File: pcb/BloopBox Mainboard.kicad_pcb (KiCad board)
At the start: 4 copper layers, 65 x 44 mm, 57 parts, among them J1 SPKR, J2 Raspberry_Pi, J3 I2C, J4 TailBoard, J5 GPIO, J6 NFCModuleV3, J7 ExtLED, Q1 2N7002, Q2 2N7002, Q3 2N7002, Q4 2N7002, Q5 2N7002, Q6 2N7002, U1 MAX98357

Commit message: feat: prepare files for automatic version numbering
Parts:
- G***, REF**: moved to B.Cu
- moved REF** 23.1 mm to (160.0, 61.2), turned to 180 degrees
- moved G*** 10.4 mm to (140.0, 61.0), turned to 180 degrees
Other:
- board text added: "BloopBox Mainboard ${VERSION} ${DATE}"
- board text added: "BloopBox Mainboard ${VERSION} %{DATE}"
- board text removed: "BloopBox v1.0"

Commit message: feat: more variables
Using more variables to automate stuff
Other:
- board text added: "${TITLE} ${VERSION} ${DATE}"
- board text removed: "BloopBox Mainboard ${VERSION} ${DATE}"
- board text removed: "BloopBox Mainboard ${VERSION} %{DATE}"
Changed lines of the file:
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@@
     )
   )
+  (property "DATE" "~DATE~")
+  (property "VERSION" "~VERSION~")
   (net 0 "")
   (net 1 "/OUTP")
@@
     (effects (font (size 1 1) (thickness 0.15)) (justify right mirror))
   )
-  (gr_text "BloopBox Mainboard\n${VERSION} %{DATE}" (at 150 55) (layer "B.SilkS")
+  (gr_text "${TITLE}\n${VERSION} ${DATE}" (at 150 55) (layer "B.SilkS")
     (effects (font (size 1.2 1.2) (thickness 0.2)) (justify mirror))
   )
@@
     (effects (font (size 0.8 0.8) (thickness 0.15)))
   )
-  (gr_text "BloopBox Mainboard\n${VERSION} ${DATE}" (at 150 42) (layer "F.SilkS")
+  (gr_text "${TITLE}\n${VERSION} ${DATE}" (at 150 42) (layer "F.SilkS")
     (effects (font (size 1.2 1.2) (thickness 0.2)))
   )

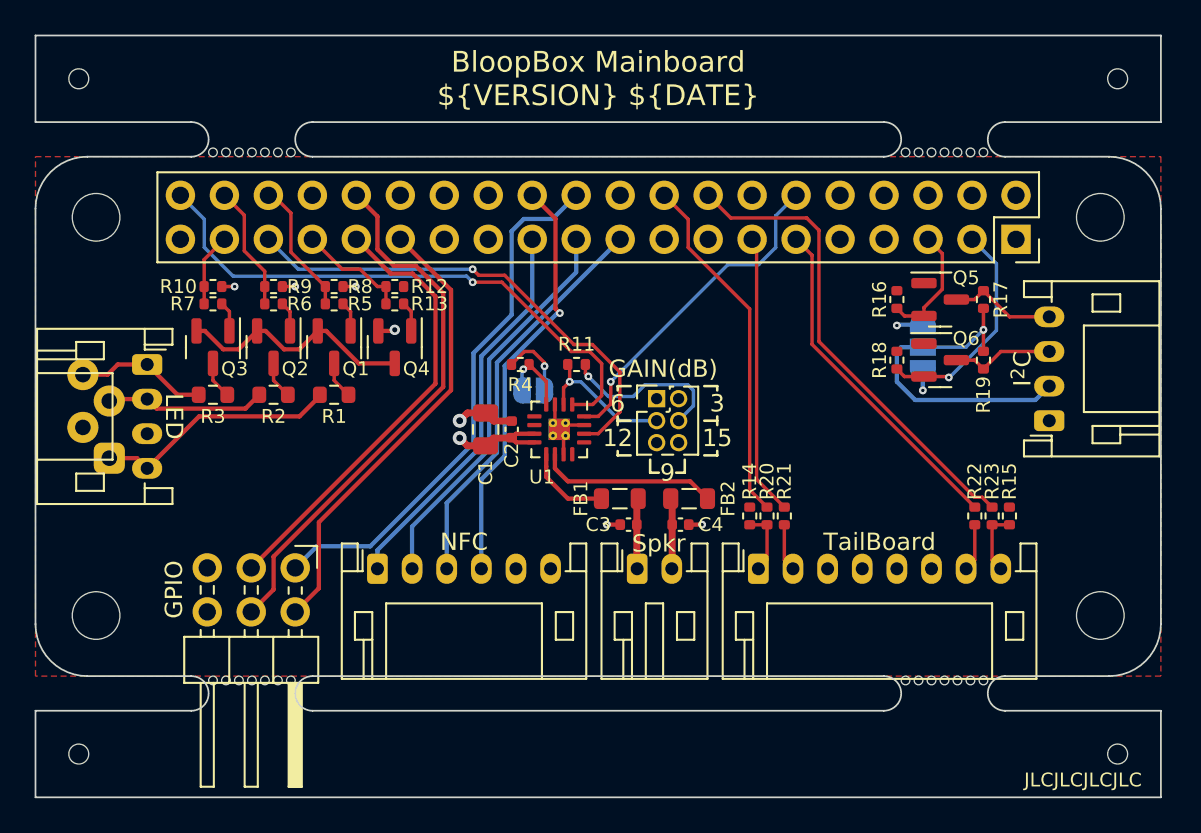
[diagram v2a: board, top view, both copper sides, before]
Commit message: feat: add UART to GPIO-Header
Adding the UART TX and RX pins to the GPIO header for debugging console access
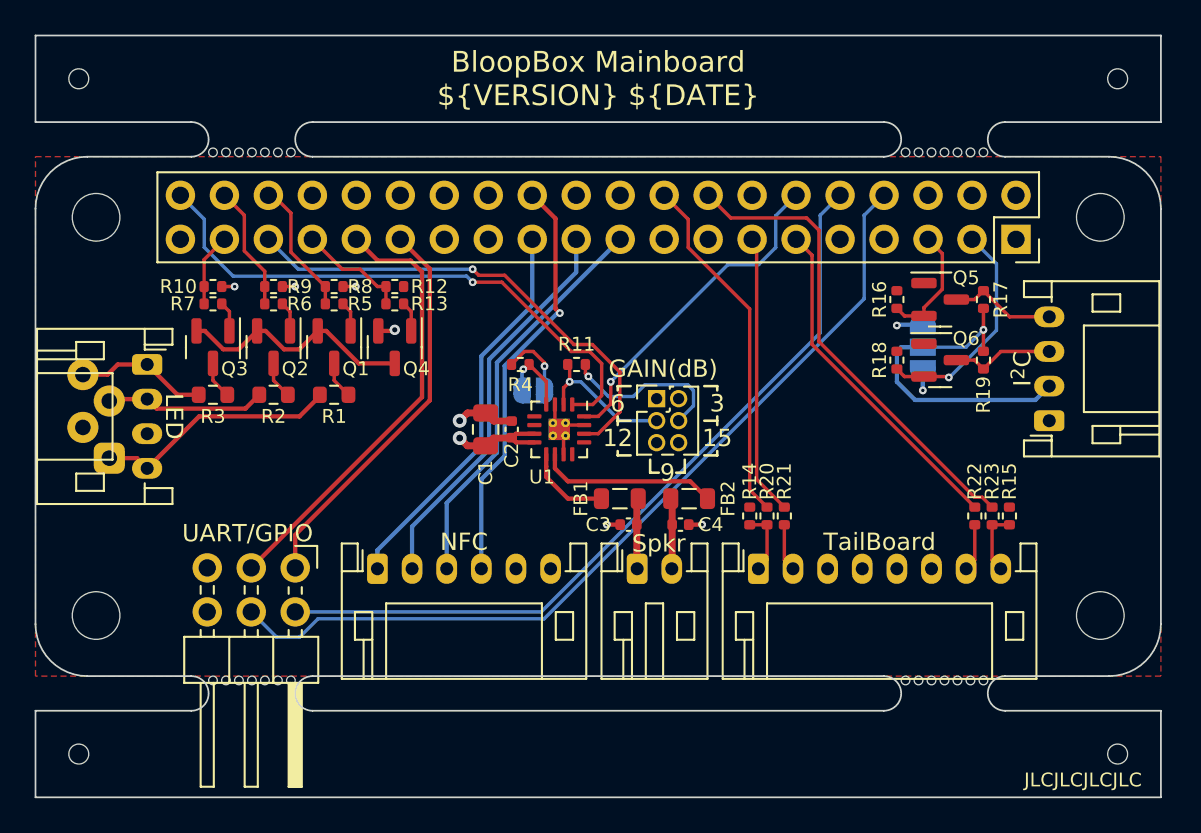
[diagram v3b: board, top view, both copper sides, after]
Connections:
- net /GPIO3 renamed /GPIO6
- J2 pad 10: unconnected-(J2-Pad10) -> /RX
- J2 pad 22: /GPIO1 -> unconnected-(J2-Pad22)
- J2 pad 29: /GPIO2 -> /GPIO5
- J2 pad 32: /GPIO4 -> unconnected-(J2-Pad32)
- J2 pad 8: unconnected-(J2-Pad8) -> /TX
- J5 pad 1: /GPIO1 -> /GPIO5
- J5 pad 2: /GPIO2 -> /RX
- J5 pad 4: /GPIO4 -> /TX
- J5 pad 5: GND -> +3V3
- J5 pad 6: +3V3 -> GND
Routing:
- net /TX: track 0.00 -> 50.6 mm
- net /RX: track 0.00 -> 45.4 mm
- net /GPIO4: track 31.5 -> 0.00 mm
- net /GPIO1: track 31.0 -> 0.00 mm
- net /GPIO2: track 26.5 -> 0.00 mm
- net /GPIO5: track 0.00 -> 22.9 mm
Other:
- board text added: "05"
- board text added: "06"
- board text added: "RX"
- board text added: "TX"
- board text added: "UART/GPIO"
- board text removed: "06 12"
- board text removed: "25 05"
- board text removed: "GPIO"
- board text removed: "IO3"
- board text removed: "IO4"

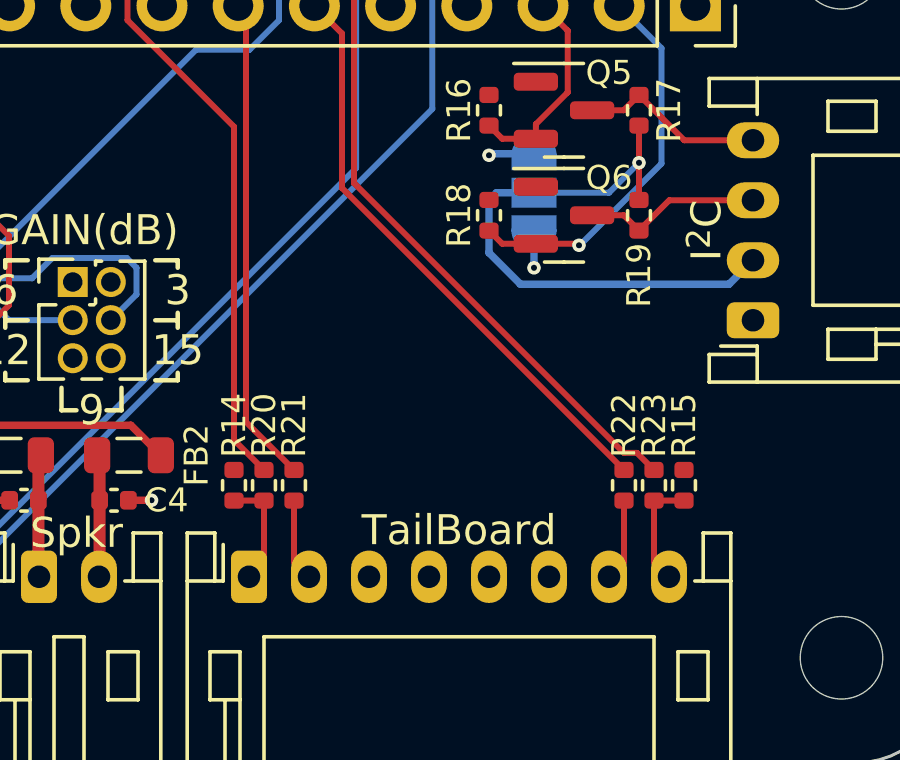
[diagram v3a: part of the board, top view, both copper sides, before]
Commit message: fix: remove Tailboard IO protection resistors
After removing the PD controller from the tailboard, the LEDs are directly connected to the mainboard so the protection resistors had to go
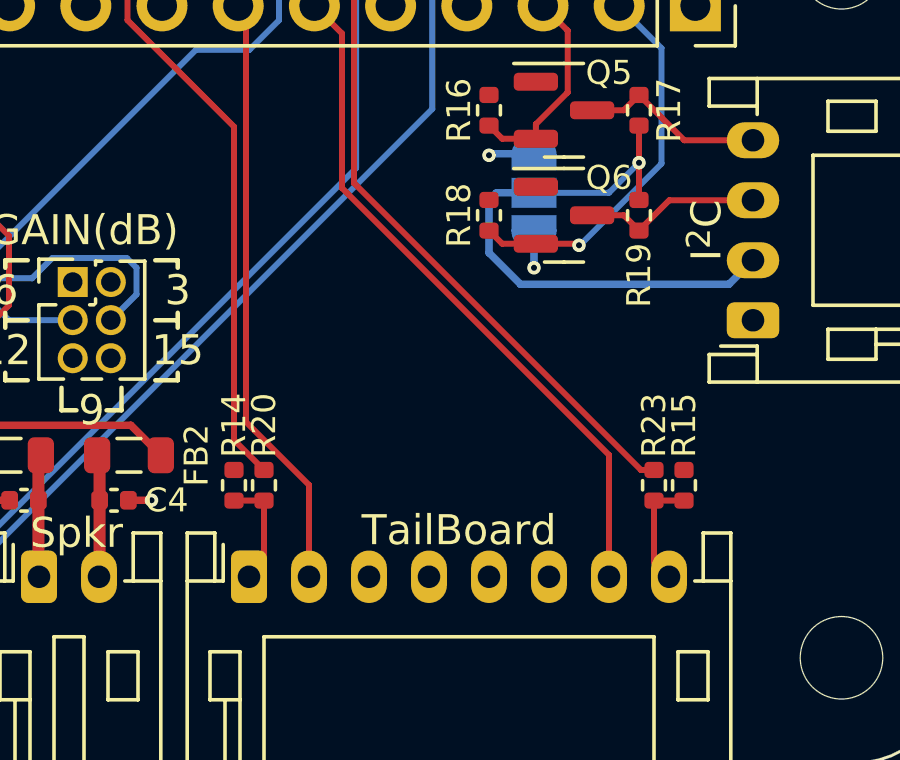
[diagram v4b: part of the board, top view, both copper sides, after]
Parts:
- removed R21, R22: 1k, Resistor_SMD:R_0402_1005Metric
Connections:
- J4 pad 2: /Tail2 -> /Tail_IO1
- J4 pad 7: /Tail7 -> /Tail_IO2
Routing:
- net /Tail_IO1: track 16.2 -> 20.0 mm
- net /Tail_IO2: track 19.7 -> 23.1 mm
- net /Tail7: track 2.75 -> 0.00 mm
- net /Tail2: track 2.75 -> 0.00 mm

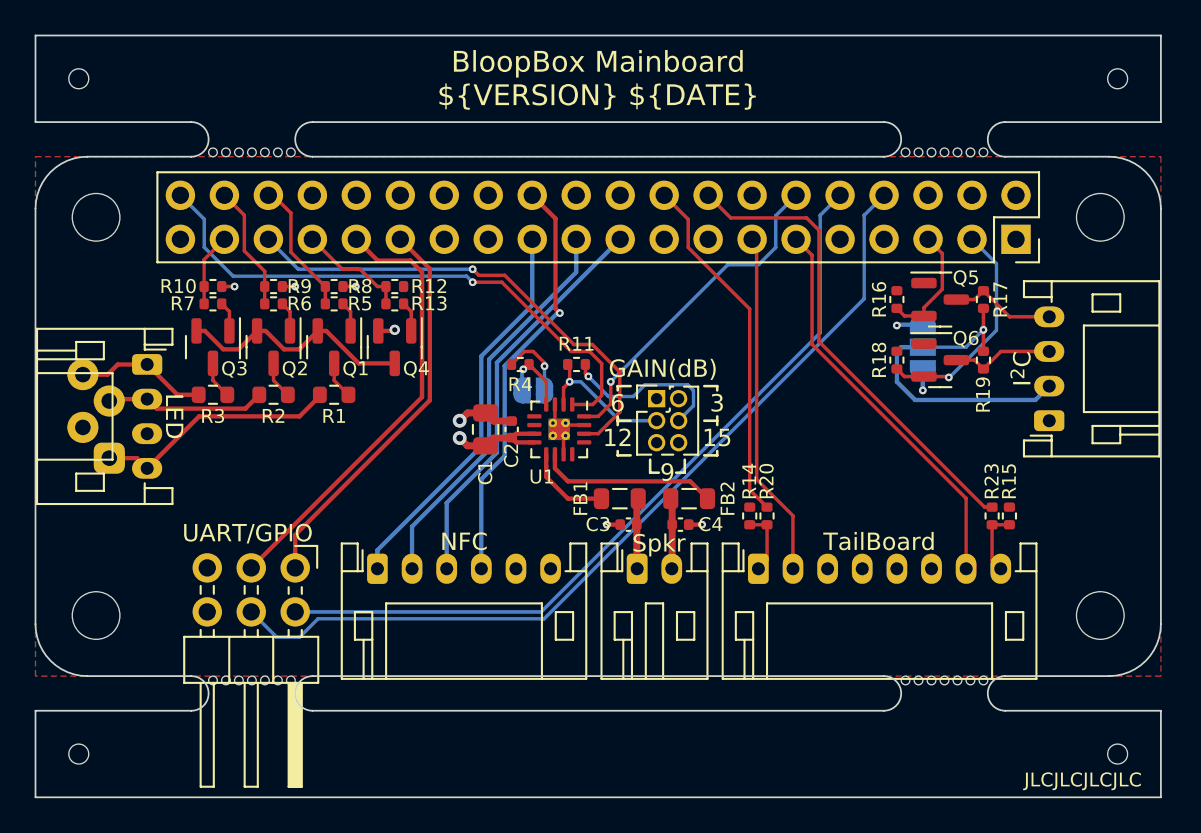
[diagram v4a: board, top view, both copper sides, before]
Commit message: feat!: change NFC connector to RC522 pinout
Switch the NFC-connector from the PN532 module to the RC522 since the PN532 works not reliable with NTAG
Connect IRQ and RST lines while doing so
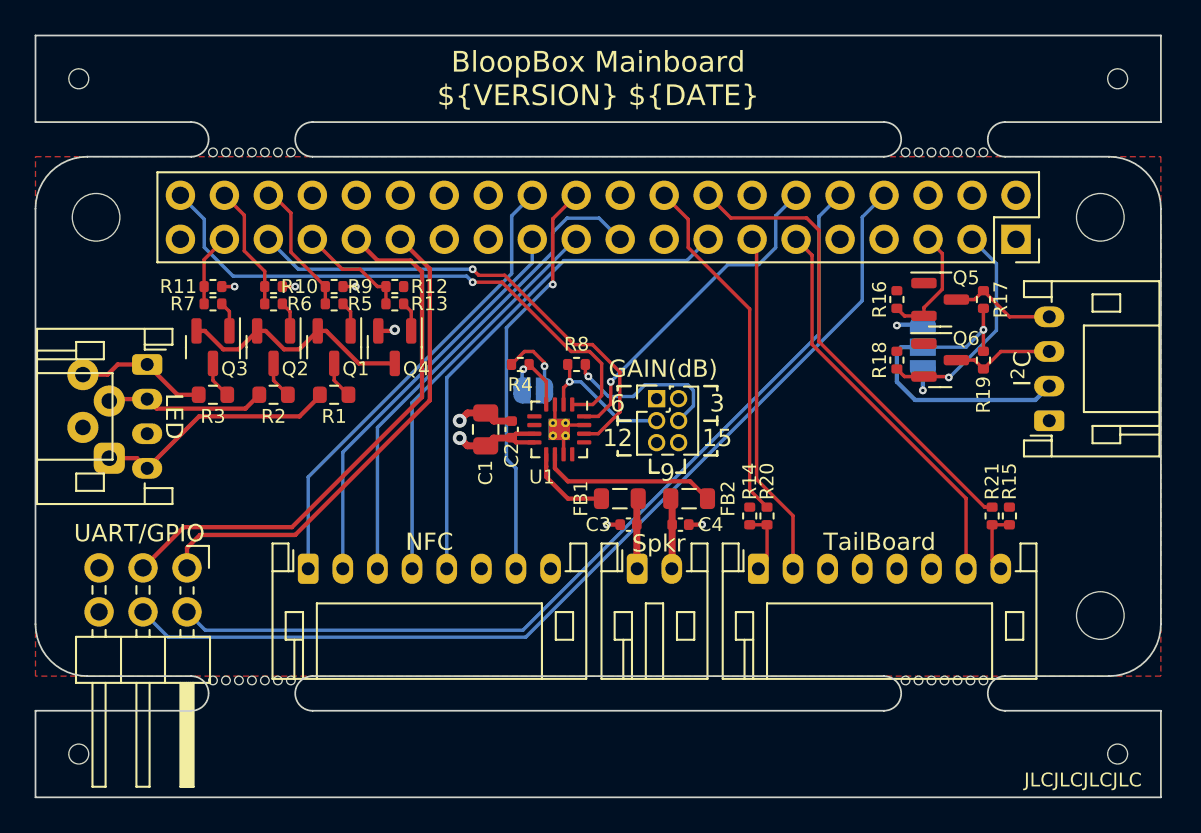
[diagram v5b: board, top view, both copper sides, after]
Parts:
- removed the J6 at (137.2, 70.3)
- added J5: NFC-Module, Connector_JST:JST_PH_S8B-PH-K_1x08_P2.00mm_Horizontal, F.Cu at (133.2, 70.3)
- moved J6 6.25 mm to (126.2, 70.2)
- renumbered J7 to J1, J1 to J2, J2 to J3, J3 to J4, J5 to J6, J4 to J7, R9 to R10, R10 to R11, R23 to R21, R11 to R8, R8 to R9
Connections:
- J3 pad 15: unconnected-(J2-Pad15) -> /NFC_IRQ
- J3 pad 19: /NFC-MOSI -> /NFC_MOSI
- J3 pad 21: /NFC-MISO -> /NFC_MISO
- J3 pad 22: unconnected-(J2-Pad22) -> /NFC_RST
- J3 pad 23: /NFC-SCK -> /NFC_SCK
- J3 pad 24: /NFC-Select -> /NFC_Select
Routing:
- net /NFC_IRQ: track 0.00 -> 29.4 mm
- net /NFC_MOSI: track 0.00 -> 28.4 mm
- net /NFC_Select: track 0.00 -> 26.9 mm
- net /NFC-Select: track 24.2 -> 0.00 mm, vias 1 -> 0
- net /NFC_RST: track 0.00 -> 23.6 mm, vias 0 -> 1
- net /NFC_SCK: track 0.00 -> 23.6 mm
- net /NFC-MOSI: track 23.2 -> 0.00 mm
- net /NFC_MISO: track 0.00 -> 23.0 mm
- net /NFC-MISO: track 23.0 -> 0.00 mm
- net /NFC-SCK: track 22.7 -> 0.00 mm
- net /RX: track 45.4 -> 52.5 mm
- net /TX: track 50.6 -> 56.8 mm
- net /GPIO6: track 25.8 -> 32.0 mm
- net /GPIO5: track 22.9 -> 28.7 mm
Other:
- board text added: "22"
- board text added: "25"
- board text added: "IRQ"
- board text added: "RST"
- board text added: "SEL"
- board text removed: "CS"

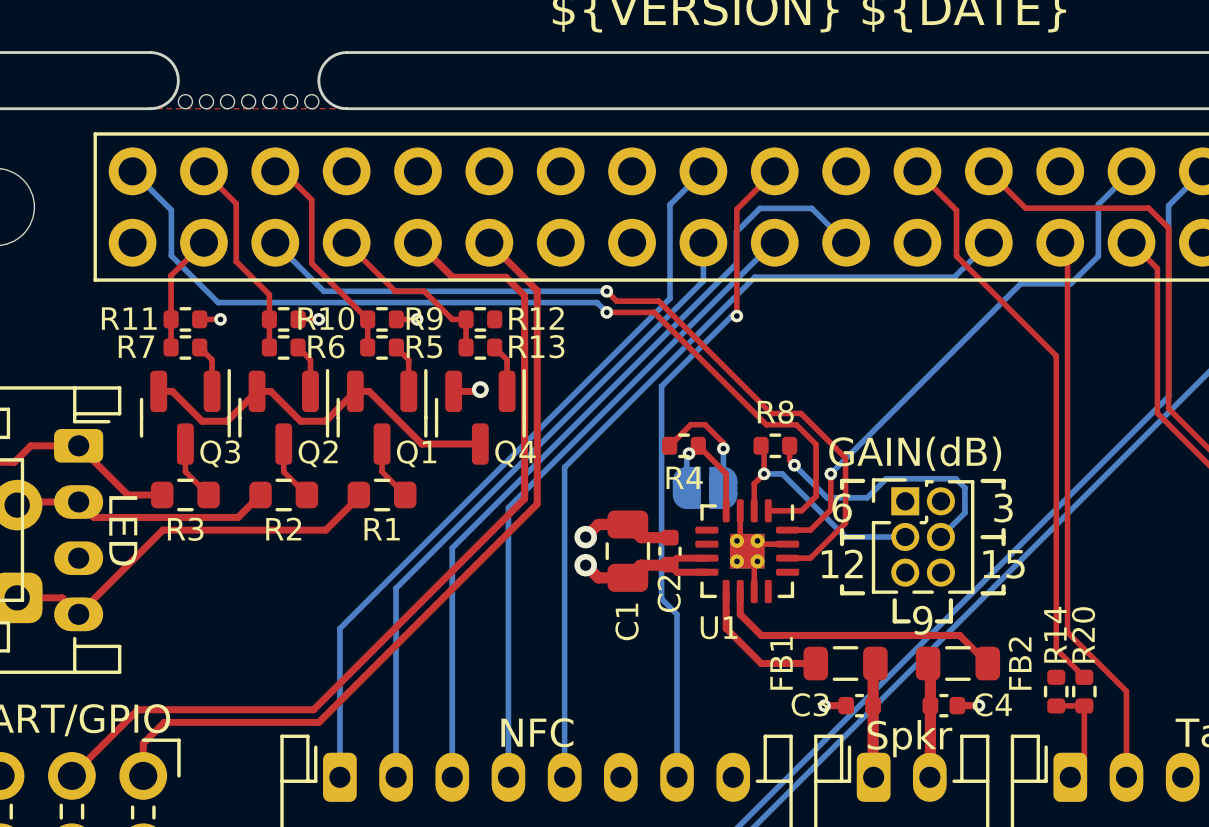
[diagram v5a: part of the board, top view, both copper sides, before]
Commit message: feat: add ID EEPROM
Add (optional) ID EEPROM to the board that will allow some of the hardware to be auto-configured on the Raspberry Pi.
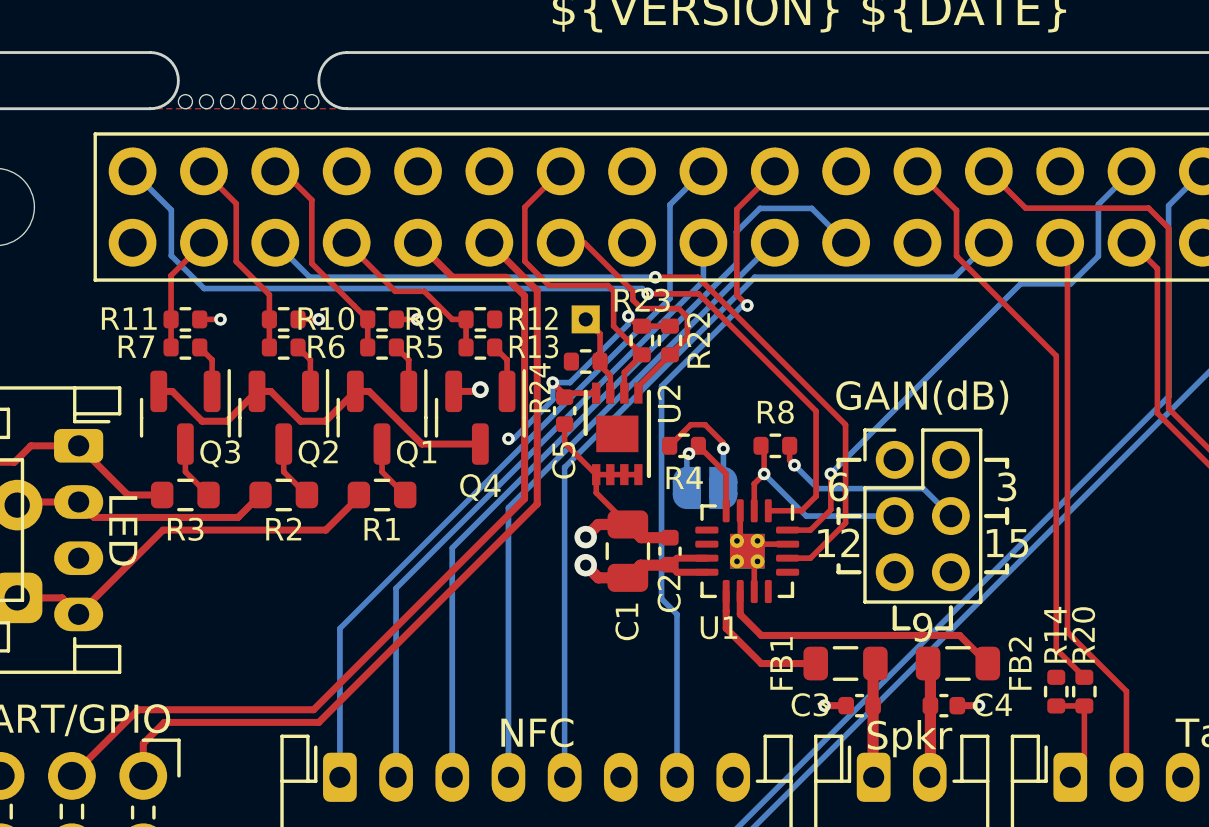
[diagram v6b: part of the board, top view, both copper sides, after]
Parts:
- added C5: 100nF, Capacitor_SMD:C_0402_1005Metric, F.Cu at (141.2, 57.2)
- added J8: PROG, TestPoint:TestPoint_THTPad_1.0x1.0mm_Drill0.5mm, B.Cu at (142.0, 54.0)
- added R22: 3k9, Resistor_SMD:R_0402_1005Metric, F.Cu at (145.0, 54.8)
- added R23: 3k9, Resistor_SMD:R_0402_1005Metric, F.Cu at (144.0, 54.8)
- added R24: 1k, Resistor_SMD:R_0402_1005Metric, F.Cu at (142.0, 55.5)
- added U2: CAT24C32, Package_DFN_QFN:DFN-8-1EP_3x2mm_P0.5mm_EP1.3x1.5mm, F.Cu at (143.1, 58.1)
- JP2: footprint Connector_PinHeader_1.27mm:PinHeader_2x03_P1.27mm_Vertical -> Connector_PinHeader_2.00mm:PinHeader_2x03_P2.00mm_Vertical
- moved REF** 31.1 mm to (128.9, 60.5)
- moved G*** 4.06 mm to (136.2, 59.7)
- moved JP2 1.52 mm to (153.0, 59.0)
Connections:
- J3 pad 27: unconnected-(J3-Pad27) -> /ID_SD
- J3 pad 28: unconnected-(J3-Pad28) -> /ID_SC
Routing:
- net /ID_SC: track 0.00 -> 11.6 mm
- net +3V3: track 1.52 -> 11.7 mm, vias 1 -> 4
- net /ID_SD: track 0.00 -> 9.21 mm
- net GND: track 11.0 -> 17.0 mm
- net /ID_WP: track 0.00 -> 2.99 mm
- net /GAINr: track 9.82 -> 7.08 mm
- net /AMP_LRCLK: track 28.4 -> 29.1 mm
- net /AMP_DIN: track 33.1 -> 33.8 mm
- net /GAIN: track 8.30 -> 7.62 mm
